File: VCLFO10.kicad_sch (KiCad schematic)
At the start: 17 parts, among them J1 Conn_02x05_Odd_Even, U1 LM7805_TO220, U2 ED_VCLFO10

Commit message: Routing done
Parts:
- removed C4, C5: 10nF, Capacitor_SMD:C_1206_3216Metric_Pad1.33x1.80mm_HandSolder, symbol Device:C
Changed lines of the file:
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@@
   (junction (at 152.4 76.2) (diameter 0) (color 0 0 0 0)
-  )
-  (junction (at 134.62 29.845) (diameter 0) (color 0 0 0 0)
   )
   (junction (at 176.53 36.195) (diameter 0) (color 0 0 0 0)
@@
     (stroke (width 0) (type default) (color 0 0 0 0))
   )
-  (wire (pts (xy 134.62 29.845) (xy 137.16 29.845))
-    (stroke (width 0) (type default) (color 0 0 0 0))
-  )
   (wire (pts (xy 127 114.3) (xy 132.08 114.3))
     (stroke (width 0) (type default) (color 0 0 0 0))
@@
     (stroke (width 0) (type default) (color 0 0 0 0))
   )
-  (wire (pts (xy 134.62 29.845) (xy 134.62 30.48))
-    (stroke (width 0) (type default) (color 0 0 0 0))
-  )
   (wire (pts (xy 165.1 34.29) (xy 165.1 36.195))
     (stroke (width 0) (type default) (color 0 0 0 0))
@@
   )
   (wire (pts (xy 176.53 36.195) (xy 187.96 36.195))
-    (stroke (width 0) (type default) (color 0 0 0 0))
-  )
-  (wire (pts (xy 134.62 28.575) (xy 134.62 29.845))
     (stroke (width 0) (type default) (color 0 0 0 0))
   )
@@
     (pin "9")
   )
-  (symbol (lib_id "Device:C") (at 134.62 24.765 0) (unit 1)
-    (in_bom yes) (on_board yes) (fields_autoplaced)
-    (property "Reference" "C4" (id 0) (at 137.541 23.8565 0)
-      (effects (font (size 1.27 1.27)) (justify left))
-    )
-    (property "Value" "10nF" (id 1) (at 137.541 26.6316 0)
-      (effects (font (size 1.27 1.27)) (justify left))
-    )
-    (property "Footprint" "Capacitor_SMD:C_1206_3216Metric_Pad1.33x1.80mm_HandSolder" (id 2) (at 135.5852 28.575 0)
-      (effects (font (size 1.27 1.27)) hide)
-    )
-    (property "Datasheet" "~" (id 3) (at 134.62 24.765 0)
-      (effects (font (size 1.27 1.27)) hide)
-    )
-    (pin "1")
-    (pin "2")
-  )
   (symbol (lib_id "My Stuff:Logo_Open_Hardware_Small") (at 184.15 172.72 0) (unit 1)
     (in_bom yes) (on_board yes) (fields_autoplaced)
@@
     (pin "1")
   )
-  (symbol (lib_id "Device:C") (at 134.62 34.29 0) (unit 1)
-    (in_bom yes) (on_board yes) (fields_autoplaced)
-    (property "Reference" "C5" (id 0) (at 137.541 33.3815 0)
-      (effects (font (size 1.27 1.27)) (justify left))
-    )
-    (property "Value" "10nF" (id 1) (at 137.541 36.1566 0)
-      (effects (font (size 1.27 1.27)) (justify left))
-    )
-    (property "Footprint" "Capacitor_SMD:C_1206_3216Metric_Pad1.33x1.80mm_HandSolder" (id 2) (at 135.5852 38.1 0)
-      (effects (font (size 1.27 1.27)) hide)
-    )
-    (property "Datasheet" "~" (id 3) (at 134.62 34.29 0)
-      (effects (font (size 1.27 1.27)) hide)
-    )
-    (pin "1")
-    (pin "2")
-  )
   (symbol (lib_id "Device:FerriteBead") (at 90.805 26.67 90) (unit 1)
     (in_bom yes) (on_board yes) (fields_autoplaced)
@@
       (effects (font (size 1.27 1.27)) hide)
     )
-  )
-  (symbol (lib_id "power:GND") (at 137.16 29.845 90) (unit 1)
-    (in_bom yes) (on_board yes) (fields_autoplaced)
-    (property "Reference" "#PWR0121" (id 0) (at 143.51 29.845 0)
-      (effects (font (size 1.27 1.27)) hide)
-    )
-    (property "Value" "GND" (id 1) (at 140.335 30.324 90)
-      (effects (font (size 1.27 1.27)) (justify right))
-    )
-    (property "Footprint" "" (id 2) (at 137.16 29.845 0)
-      (effects (font (size 1.27 1.27)) hide)
-    )
-    (property "Datasheet" "" (id 3) (at 137.16 29.845 0)
-      (effects (font (size 1.27 1.27)) hide)
-    )
-    (pin "1")
   )
   (symbol (lib_id "power:PWR_FLAG") (at 268.605 25.4 0) (unit 1)
@@
     (pin "1")
   )
-  (symbol (lib_id "power:+12V") (at 134.62 20.955 0) (unit 1)
-    (in_bom yes) (on_board yes) (fields_autoplaced)
-    (property "Reference" "#PWR0129" (id 0) (at 134.62 24.765 0)
-      (effects (font (size 1.27 1.27)) hide)
-    )
-    (property "Value" "+12V" (id 1) (at 134.62 17.3505 0))
-    (property "Footprint" "" (id 2) (at 134.62 20.955 0)
-      (effects (font (size 1.27 1.27)) hide)
-    )
-    (property "Datasheet" "" (id 3) (at 134.62 20.955 0)
-      (effects (font (size 1.27 1.27)) hide)
-    )
-    (pin "1")
-  )
   (symbol (lib_id "power:-12V") (at 94.615 26.67 270) (unit 1)
     (in_bom yes) (on_board yes) (fields_autoplaced)
@@
     (pin "1")
     (pin "2")
-  )
-  (symbol (lib_id "power:-12V") (at 134.62 38.1 180) (unit 1)
-    (in_bom yes) (on_board yes) (fields_autoplaced)
-    (property "Reference" "#PWR0120" (id 0) (at 134.62 40.64 0)
-      (effects (font (size 1.27 1.27)) hide)
-    )
-    (property "Value" "-12V" (id 1) (at 134.62 42.6625 0))
-    (property "Footprint" "" (id 2) (at 134.62 38.1 0)
-      (effects (font (size 1.27 1.27)) hide)
-    )
-    (property "Datasheet" "" (id 3) (at 134.62 38.1 0)
-      (effects (font (size 1.27 1.27)) hide)
-    )
-    (pin "1")
   )
   (symbol (lib_id "power:GND") (at 34.29 31.75 270) (unit 1)
@@
       (reference "#PWR0113") (unit 1) (value "-12V") (footprint "")
     )
-    (path "/fbee022f-745e-4b8c-b30a-a1f435e3664b"
-      (reference "#PWR0120") (unit 1) (value "-12V") (footprint "")
-    )
-    (path "/830151f5-6606-41bf-8604-94eb5300ff25"
-      (reference "#PWR0121") (unit 1) (value "GND") (footprint "")
-    )
     (path "/271a057e-81fd-43e1-b800-461632f55a88"
       (reference "#PWR0122") (unit 1) (value "-12V") (footprint "")
@@
       (reference "#PWR0128") (unit 1) (value "GND") (footprint "")
     )
-    (path "/bf66660f-8621-44f2-96b7-8610b4ebe3fd"
-      (reference "#PWR0129") (unit 1) (value "+12V") (footprint "")
-    )
     (path "/190b759a-39a9-4314-b913-876ab5e65b73"
       (reference "#PWR0130") (unit 1) (value "+12V") (footprint "")
@@
       (reference "C3") (unit 1) (value "220nF") (footprint "Capacitor_SMD:C_1206_3216Metric_Pad1.33x1.80mm_HandSolder")
     )
-    (path "/225b1d70-9e04-4d1a-a1ea-febf4e2f84e5"
-      (reference "C4") (unit 1) (value "10nF") (footprint "Capacitor_SMD:C_1206_3216Metric_Pad1.33x1.80mm_HandSolder")
-    )
-    (path "/3ac1ae5e-b7e4-4d5a-bb13-8ab9d19edc26"
-      (reference "C5") (unit 1) (value "10nF") (footprint "Capacitor_SMD:C_1206_3216Metric_Pad1.33x1.80mm_HandSolder")
-    )
     (path "/a3506ddd-9a9a-4caf-a70e-11887d032402"
       (reference "C6") (unit 1) (value "100nF") (footprint "Capacitor_SMD:C_1206_3216Metric_Pad1.33x1.80mm_HandSolder")
@@
     )
     (path "/88244e95-2318-49c3-9fd7-874b4be946e2/e07d32e9-6abc-4b88-ba3a-2156fcbbcbb5"
-      (reference "J_LFO_RANGE1") (unit 1) (value "Conn_01x05") (footprint "Connector_PinSocket_2.54mm:PinSocket_1x05_P2.54mm_Horizontal")
+      (reference "J_LFO_RANGE1") (unit 1) (value "Conn_01x05") (footprint "My Stuff:PinSocket_1x05_P2.54mm_Horizontal_no_silkscreen")
     )
     (path "/88244e95-2318-49c3-9fd7-874b4be946e2/ff3b0c4e-889c-4f84-9367-627ae70df7d0"
@@
     )
     (path "/88244e95-2318-49c3-9fd7-874b4be946e2/006adfb9-d400-4da2-aa9c-9bac92905516"
-      (reference "J_SYNC_MODE1") (unit 1) (value "Conn_01x05") (footprint "Connector_PinSocket_2.54mm:PinSocket_1x05_P2.54mm_Horizontal")
+      (reference "J_SYNC_MODE1") (unit 1) (value "Conn_01x05") (footprint "My Stuff:PinSocket_1x05_P2.54mm_Horizontal_no_silkscreen")
     )
     (path "/88244e95-2318-49c3-9fd7-874b4be946e2/29cca5b2-b8b6-4eaa-8b5c-f3aa4477f1f9"

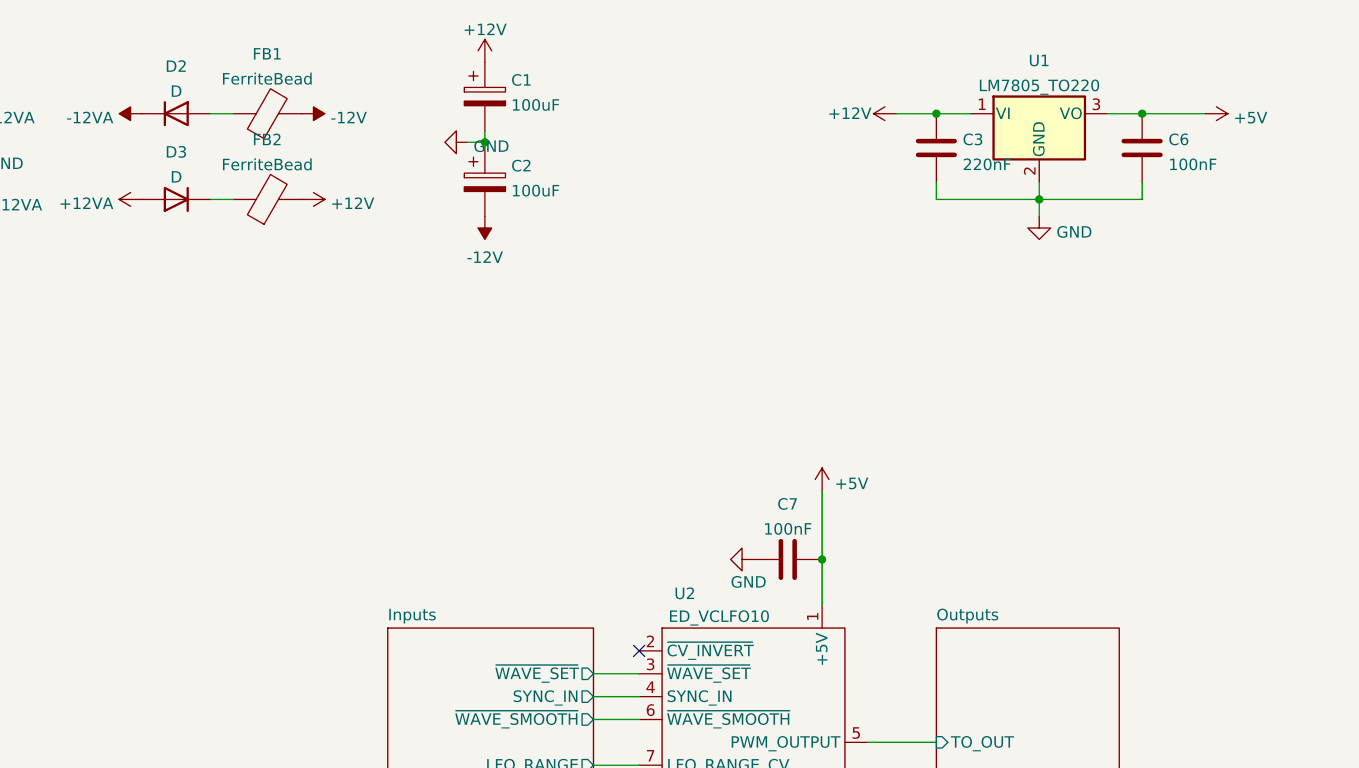
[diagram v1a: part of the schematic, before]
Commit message: Geographic reannotate and silkscreen cleanup
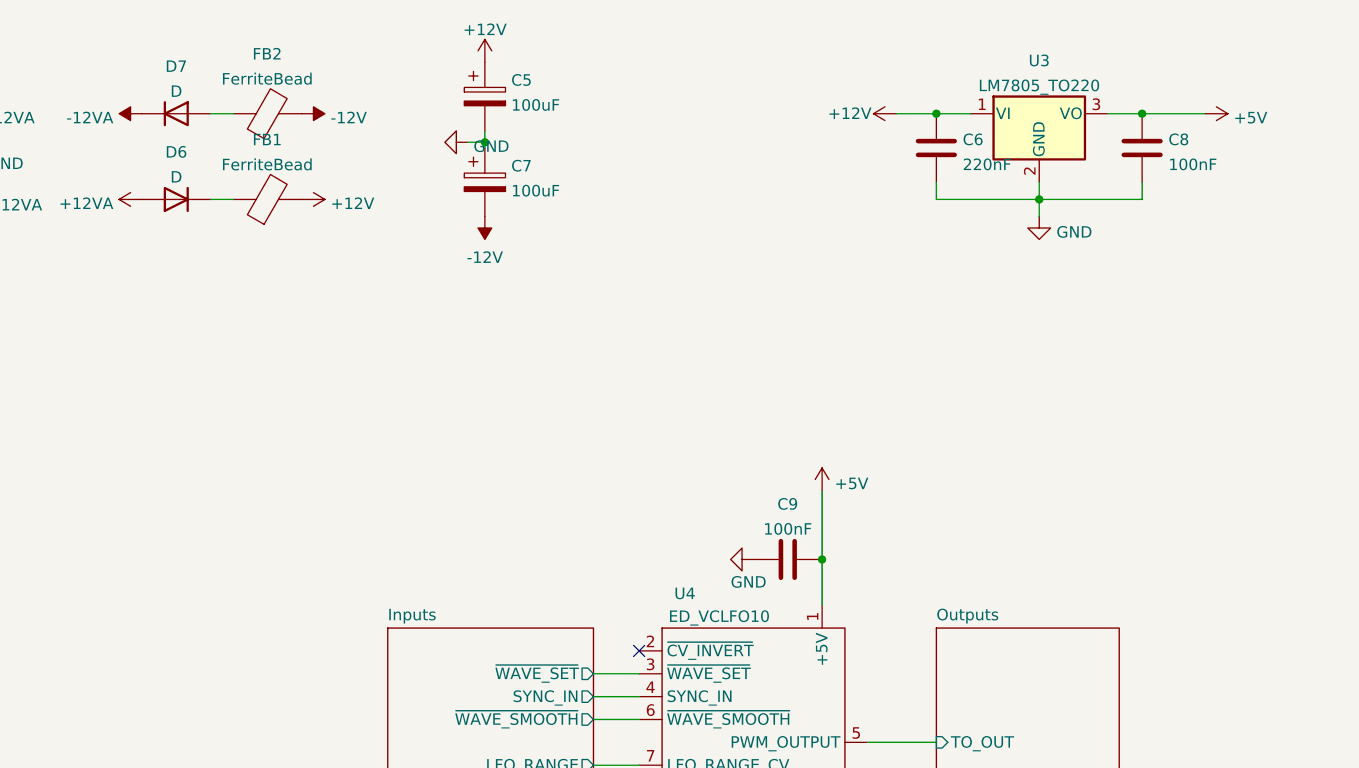
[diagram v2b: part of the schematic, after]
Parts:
- renumbered C1 to C5, C3 to C6, C2 to C7, C6 to C8, C7 to C9, D3 to D6, D2 to D7, FB2 to FB1, FB1 to FB2, U1 to U3, U2 to U4

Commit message: Update title block on schematic and pcb sheets
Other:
- title: ED VCLFO -> VCLFO10
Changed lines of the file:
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@@
   (paper "A4")
   (title_block
-    (title "ED VCLFO")
-    (date "2022-05-15")
+    (title "VCLFO10")
+    (date "2022-06-29")
     (rev "1.0")
     (company "RobotDialogs")
